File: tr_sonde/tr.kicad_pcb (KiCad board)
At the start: 4 copper layers, 108.2 x 67.3 mm, 90 parts, among them J1 SMA, J2 SMA, J3 SMA, K1 SMDHDR, K2 SMDHDR, K3 SMDHDR, Q1 PBSS4250X, Q2 MMBT2222A, Q3 STD2NK90ZT4, Q4 STD2NK90ZT4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

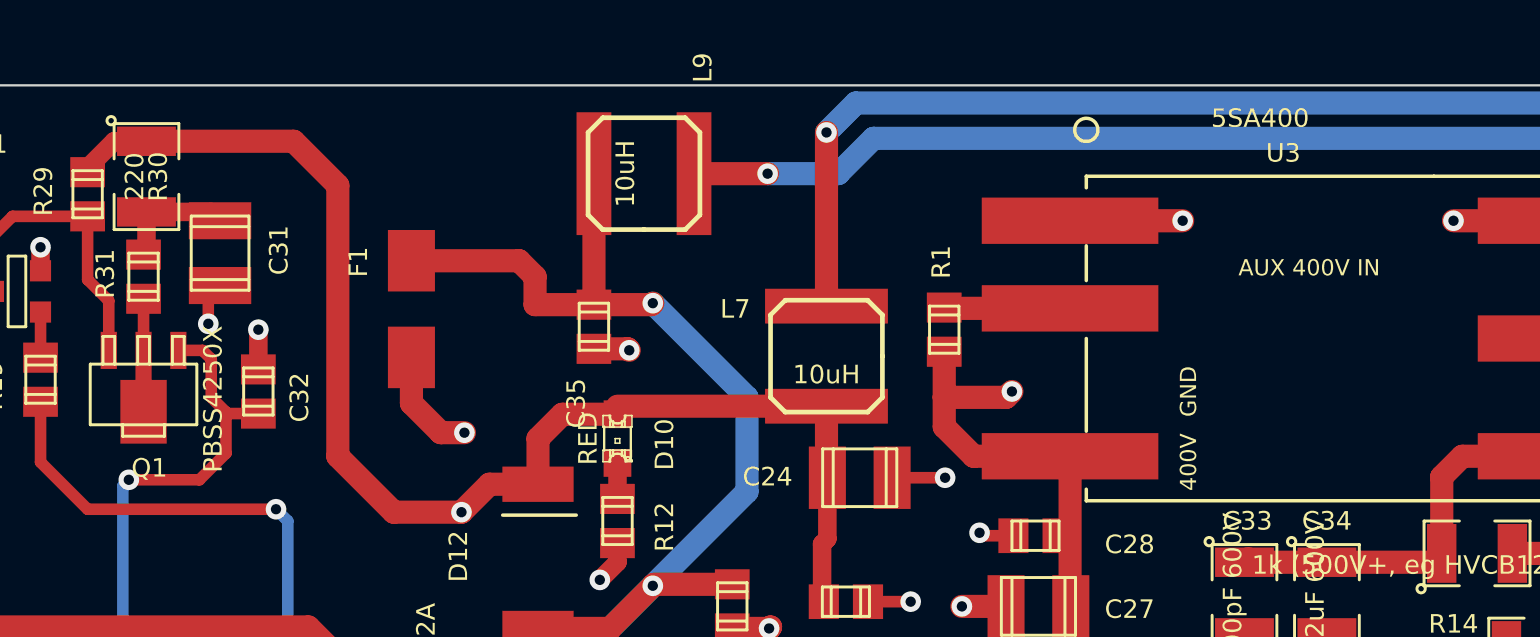
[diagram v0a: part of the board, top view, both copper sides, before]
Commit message: shrank power distro board for mounting on plate, updated transmitter plate drawings
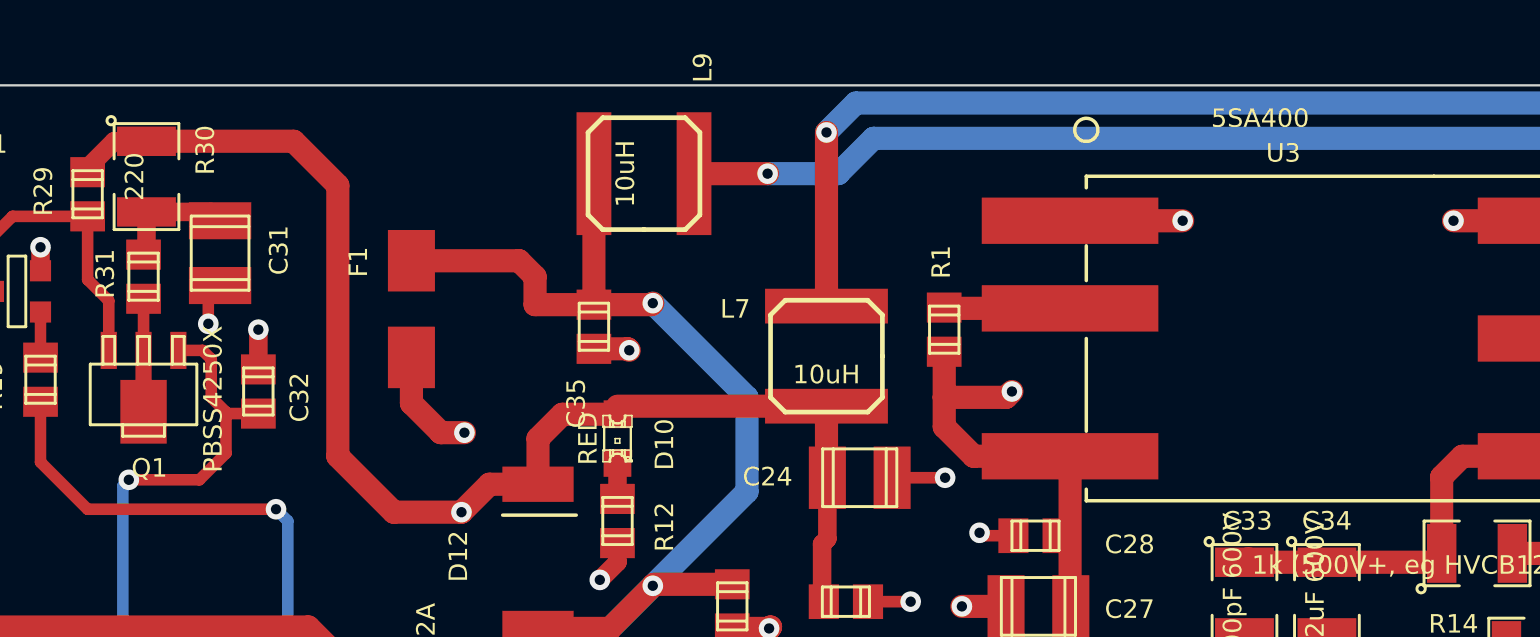
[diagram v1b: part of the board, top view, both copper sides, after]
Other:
- board text removed: "400V"
- board text removed: "AUX 400V IN"
- board text removed: "GND"

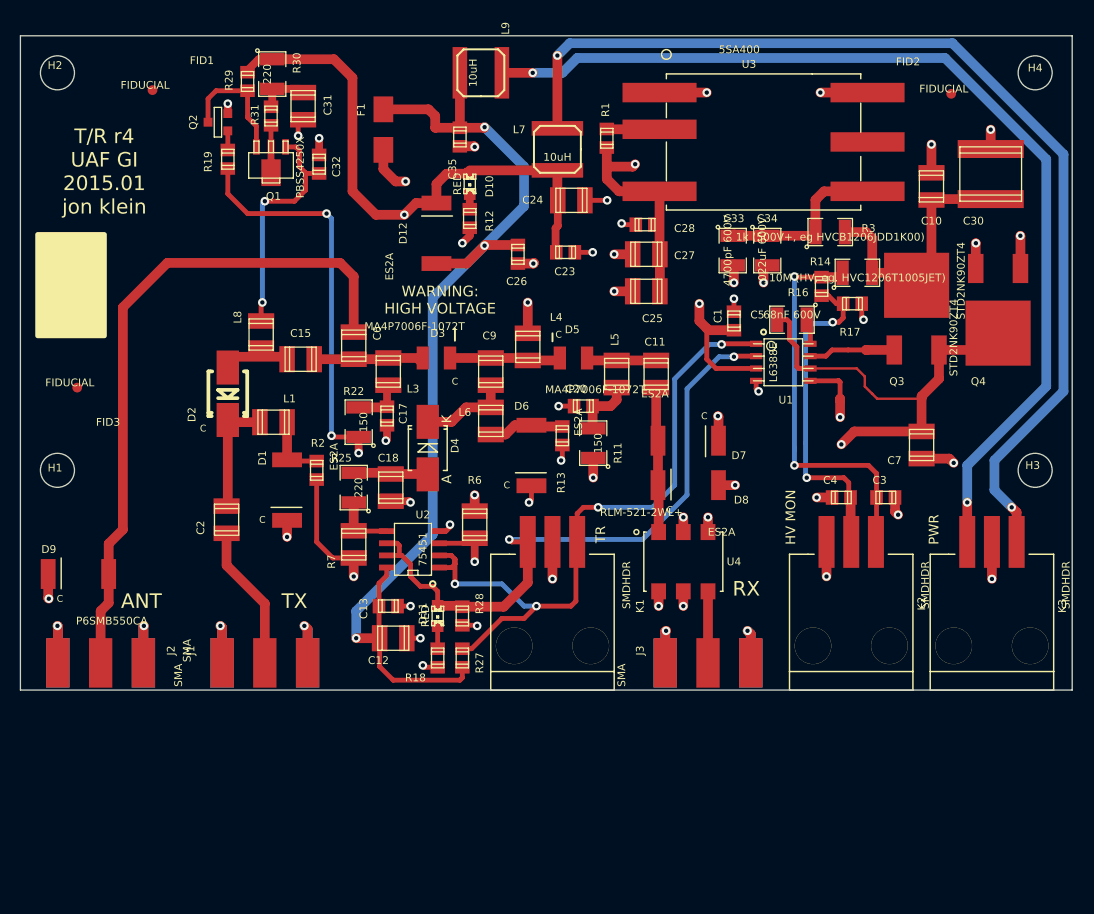
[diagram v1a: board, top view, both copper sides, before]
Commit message: added scripts for using gerbmerge for panelizing boards to reduce assembly costs
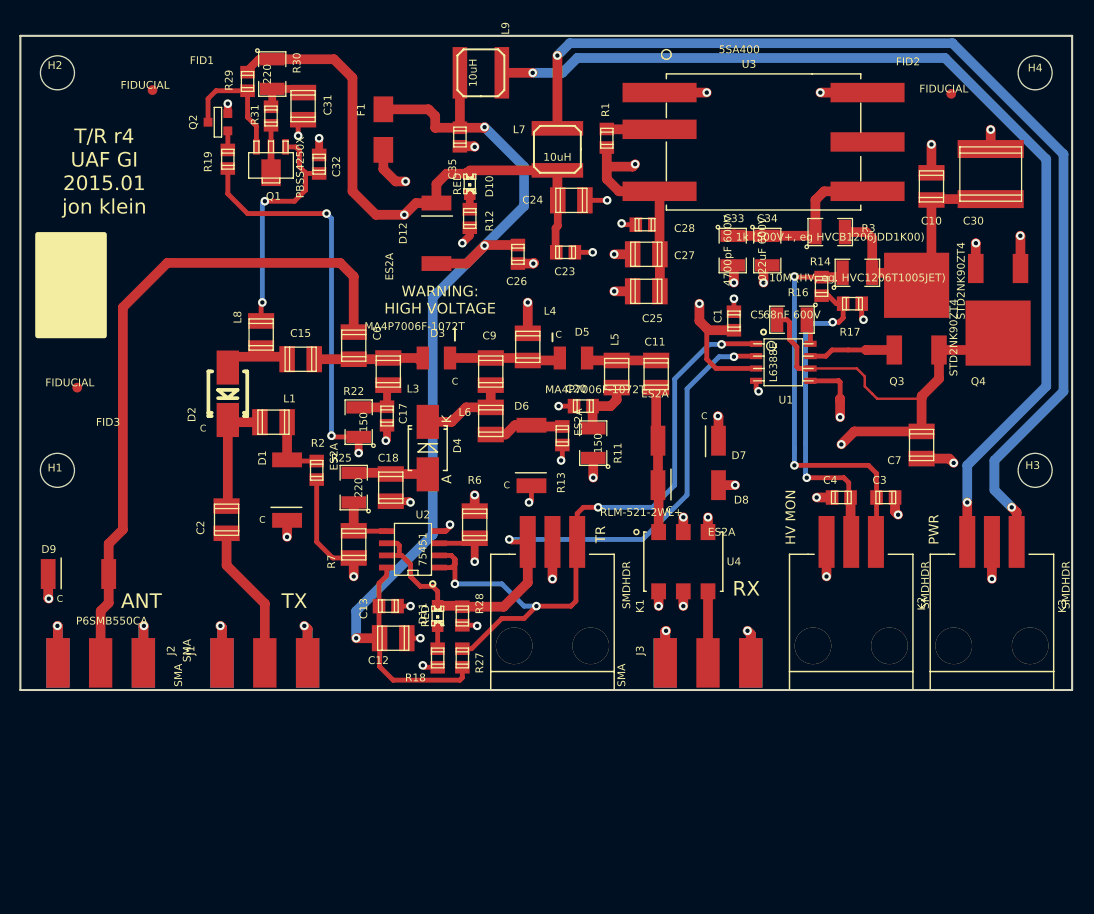
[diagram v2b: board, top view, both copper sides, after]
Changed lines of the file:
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@@
     (area 54.753358 21.844 166.370001 92.710001)
     (thickness 1.6)
-    (drawings 25)
+    (drawings 29)
     (tracks 584)
     (zones 0)
@@
   (layers
     (15 F.Cu signal)
-    (2 Inner2.Cu signal hide)
+    (2 Inner2.Cu signal)
     (1 Inner1.Cu signal)
     (0 B.Cu signal)
@@
   )
   (setup
-    (last_trace_width 0.5)
+    (last_trace_width 0.18)
     (user_trace_width 0.5)
     (user_trace_width 0.8)
@@
     (user_trace_width 2.54)
     (trace_clearance 0.17)
-    (zone_clearance 1)
+    (zone_clearance 0.5)
     (zone_45_only yes)
     (trace_min 0.18)
@@
   (module melf-1072:MELF-1072 (layer F.Cu)
     (at 113.284 57.277 180)
-    (fp_text reference D5 (at 0.127 2.921 180) (layer F.SilkS)
+    (fp_text reference D5 (at -0.889 2.667 180) (layer F.SilkS)
       (effects (font (size 0.8 0.8) (thickness 0.175)))
     )
@@
     (at 108.585 56.134 270)
     (descr "SMT capacitor, 1210")
-    (fp_text reference L4 (at -3.048 -2.921 360) (layer F.SilkS)
+    (fp_text reference L4 (at -3.683 -2.286 360) (layer F.SilkS)
       (effects (font (size 0.8 0.8) (thickness 0.175)))
     )
@@
     (tags "Diode SMB Handsoldering")
     (attr smd)
-    (fp_text reference D4 (at 0.254 2.794 90) (layer F.SilkS)
+    (fp_text reference D4 (at 0.254 3.048 90) (layer F.SilkS)
       (effects (font (size 0.8 0.8) (thickness 0.175)))
     )
@@
     (pad 5 thru_hole circle (at 3.935 -10.69 180) (size 3.78 3.78) (drill 3.76) (layers *.Cu *.Mask F.SilkS))
   )
+  (gr_line (start 56.388 91.44) (end 56.388 24.13) (angle 90) (layer F.SilkS) (width 0.2))
+  (gr_line (start 164.592 91.44) (end 56.388 91.44) (angle 90) (layer F.SilkS) (width 0.2))
+  (gr_line (start 164.592 24.13) (end 164.592 91.44) (angle 90) (layer F.SilkS) (width 0.2))
+  (gr_line (start 56.388 24.13) (end 164.592 24.13) (angle 90) (layer F.SilkS) (width 0.2))
   (gr_text C (at 60.452 82.042) (layer F.SilkS)
     (effects (font (size 0.7 0.7) (thickness 0.175)))
@@
     (polygon
       (pts
-        (xy 166.37 92.71) (xy 55.88 92.71) (xy 55.88 21.844) (xy 166.37 21.844)
+        (xy 164.592 91.44) (xy 56.769 91.44) (xy 56.769 24.13) (xy 164.592 24.13)
       )
     )

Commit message: DFM changes after last protoype rev
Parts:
- removed C10: 4700pF 600V, smd_capacitors:c_1210
- removed C25: 22uF, smd_capacitors:c_1210
- removed C26: 100nF, smd_capacitors:c_0805
- removed C33: 4700pF 600V, SMD_Packages:SMD-1210
- added C8: .022uF 600V, smd_capacitors:c_1210, F.Cu at (150.3, 39.4)
- added R10: 10k, smd_capacitors:c_0805, F.Cu at (132.7, 66.7)
- added R15: 10k, smd_capacitors:c_0805, F.Cu at (136.7, 70.5)
- added R20: 10k, smd_capacitors:c_0805, F.Cu at (139.2, 70.5)
- added R21: 150, smd_capacitors:c_1210, F.Cu at (103.8, 70.9)
- added R23: 150, smd_capacitors:c_1210, F.Cu at (87.2, 79.2)
- added R4: 1k, smd_capacitors:c_0805, F.Cu at (75.7, 28.2)
- added R5: 22, smd_capacitors:c_0805, F.Cu at (90.6, 35.4)
- added R8: 22, smd_capacitors:c_0805, F.Cu at (90.6, 30.7)
- added R9: 10k, smd_capacitors:c_0805, F.Cu at (132.7, 64.5)
- C1, C13: value 100nF -> 10nF
- D6, D7, D8, D9: footprint smb_diode:SMB_DO2144AA -> SMD_Packages:DO-214-AA_SMB
- R14: footprint SMD_Packages:SM1210 -> SMD_Packages:SMD-1206_Pol
- R16: value 3k3 -> 10k
- R17: value 15k -> 10k
- R25, R30: value 220 -> 150
- R29: value 510 -> 1k
- R6, R7: value 300 (1W) -> 150
- moved R17 22.3 mm to (133.1, 72.1)
- moved R16 20.0 mm to (132.7, 69.0), turned to 180 degrees
- moved R2 3.69 mm to (86.6, 65.2), turned to 270 degrees
- moved R14 2.43 mm to (140.1, 48.8)
- moved F1 2.38 mm to (96.1, 34.1)
- moved K2 1.91 mm to (142.0, 78.1)
- moved K1 1.91 mm to (111.1, 78.1)
- moved K3 1.91 mm to (156.3, 78.1)
- moved R6 1.65 mm to (103.8, 75.9)
- moved R29 1.53 mm to (78.4, 28.2)
- moved C4 1.35 mm to (141.9, 70.7), turned to 270 degrees
- moved C3 1.35 mm to (144.4, 70.7), turned to 270 degrees
- moved D8 1.09 mm to (124.1, 70.0)
- moved D7 1.02 mm to (124.1, 65.7)
- moved FID3 0.89 mm to (61.3, 60.3)
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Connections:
- R17 pad 2: GND -> Net-(R15-Pad1)
- R30 pad 1: VCC -> Net-(R30-Pad1)
- R6 pad 2: VCC -> Net-(R21-Pad1)
- R7 pad 2: VCC -> Net-(R23-Pad1)
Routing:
- net VCC: track 182.7 -> 202.9 mm, vias 5 -> 7
- net Net-(R30-Pad1): track 0.00 -> 10.7 mm
- net Net-(C3-Pad1): track 40.8 -> 50.6 mm, vias 2 -> 3
- net GND: track 136.4 -> 129.9 mm, vias 50 -> 48
- net Net-(C27-Pad1): track 55.0 -> 49.3 mm
- net Net-(R15-Pad1): track 0.00 -> 5.43 mm
- net +5V: track 111.4 -> 107.0 mm
- net Net-(C34-Pad1): track 17.9 -> 14.1 mm
- net Net-(R23-Pad1): track 0.00 -> 3.43 mm
- net Net-(R5-Pad2): track 0.00 -> 2.79 mm
- net Net-(R21-Pad1): track 0.00 -> 2.29 mm
- net VDD: track 39.9 -> 41.9 mm
- net /RX: track 70.7 -> 68.9 mm
- net Net-(Q1-Pad3): track 13.0 -> 14.6 mm
- net /TX: track 67.6 -> 66.1 mm
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
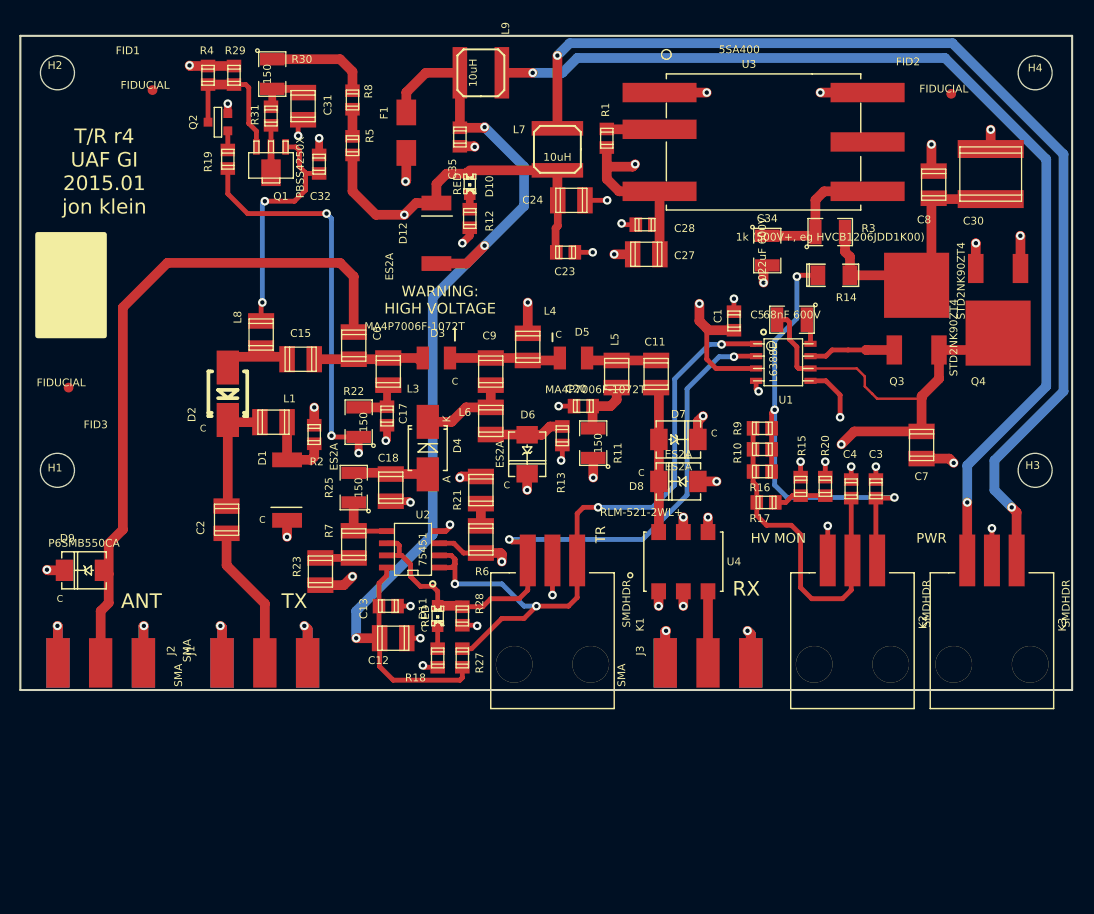
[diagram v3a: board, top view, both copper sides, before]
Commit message: simplified hptr pin diode biasing.. using a sn75372 might be fun for the next redesign
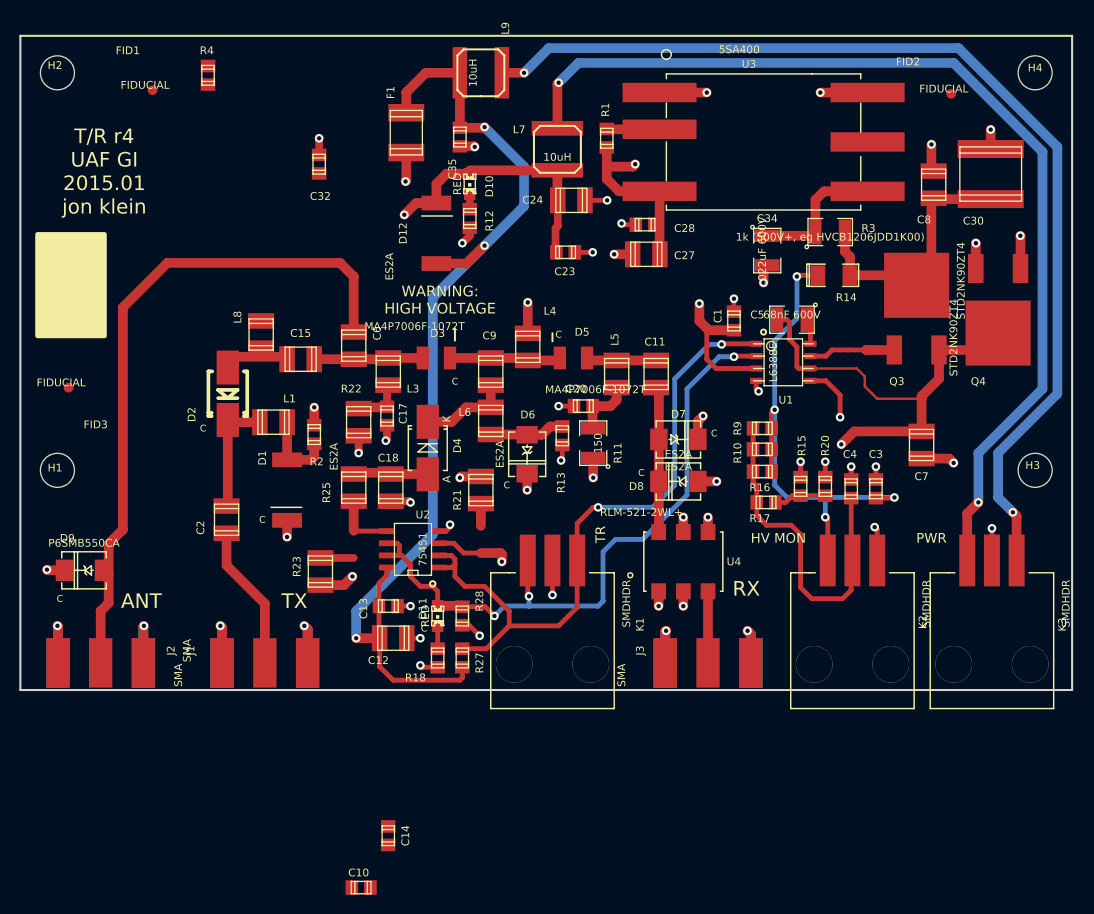
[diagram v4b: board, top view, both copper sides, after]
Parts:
- removed C31: 22uF, smd_capacitors:c_1210
- removed Q1: PBSS4250X, Transistors_SMD:sot89
- removed Q2: MMBT2222A, SMD_Packages:SOT23EBC
- removed R19: 10k, smd_capacitors:c_0805
- removed R29: 1k, smd_capacitors:c_0805
- removed R30: 150, SMD_Packages:SMD-1210
- removed R31, R5, R8: 22, smd_capacitors:c_0805
- removed R6, R7: 150, smd_capacitors:c_1210
- added C10: 10nF, smd_capacitors:c_0805, F.Cu at (91.4, 111.8)
- added C14: 10nF, smd_capacitors:c_0805, F.Cu at (94.2, 106.4)
- F1: value PTC FUSE (0ZCJ0010FF2E) -> PTC FUSE (1A TRIP); footprint Fuse_Holders_and_Fuses:Fuse_SMD1206_HandSoldering -> smd_capacitors:c_1812
- R22, R25: footprint SMD_Packages:SMD-1210 -> smd_capacitors:c_1210
- R4: value 1k -> 150
- turned F1 to 90 degrees
- turned R22 to 270 degrees
- turned R25 to 270 degrees
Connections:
- K2 pad 1: Net-(C3-Pad1) -> GND
- K2 pad 3: GND -> Net-(C3-Pad1)
- L7 pad 1: Net-(K3-Pad1) -> Net-(K3-Pad3)
- L9 pad 1: Net-(K3-Pad3) -> Net-(K3-Pad1)
- R21 pad 1: Net-(R21-Pad1) -> /RXDRV
- R23 pad 1: Net-(R23-Pad1) -> /TXDRV
- R4 pad 1: VCC -> /TXDRV
- R4 pad 2: Net-(Q1-Pad3) -> Net-(C32-Pad2)
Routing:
- net VCC: track 202.9 -> 154.3 mm, vias 7 -> 6
- net /RXDRV: track 97.4 -> 60.2 mm, vias 5 -> 3
- net Net-(C32-Pad2): track 24.5 -> 0.08 mm, vias 2 -> 0
- net Net-(Q1-Pad3): track 14.6 -> 0.00 mm
- net Net-(R30-Pad1): track 10.7 -> 0.00 mm
- net Net-(C31-Pad1): track 5.68 -> 0.00 mm
- net Net-(Q1-Pad2): track 4.88 -> 0.00 mm
- net /TX: track 66.1 -> 70.0 mm, vias 2 -> 3
- net Net-(R23-Pad1): track 3.43 -> 0.00 mm
- net /TXDRV: track 6.33 -> 9.76 mm
- net Net-(R5-Pad2): track 2.79 -> 0.00 mm
- net Net-(R21-Pad1): track 2.29 -> 0.00 mm
- net Net-(Q2-Pad2): track 1.97 -> 0.00 mm
- net Net-(C3-Pad1): track 50.6 -> 52.5 mm, vias 3 -> 4
- net GND: track 129.9 -> 128.5 mm, vias 48 -> 46
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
